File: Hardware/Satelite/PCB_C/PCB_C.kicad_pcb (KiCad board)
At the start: 2 copper layers, 54 x 54 mm, 50 parts, among them IC1 MCP1501T-33E_CHY, IC2 IS25LP080D-JULE-TR, IC3 BQ24392RSER, IC4 MS563702BA03-50, IC5 BMX055, J1 Conn_01x06, J2 JUMPER, J3 Conector_PCB_B-C, J4 Conector_Expansion_CanSat, J5 USB_B_Micro, Q1 BC817, U1 NTB0104BQ,115, U2 TCA9802DGKR, U3 STM32F303RETx, U4 NTB0104BQ,115, U5 SN74LVC1G3157DCKR, U6 Si7006-A20-IM1, Y1 LFXTAL016178, Y2 Crystal

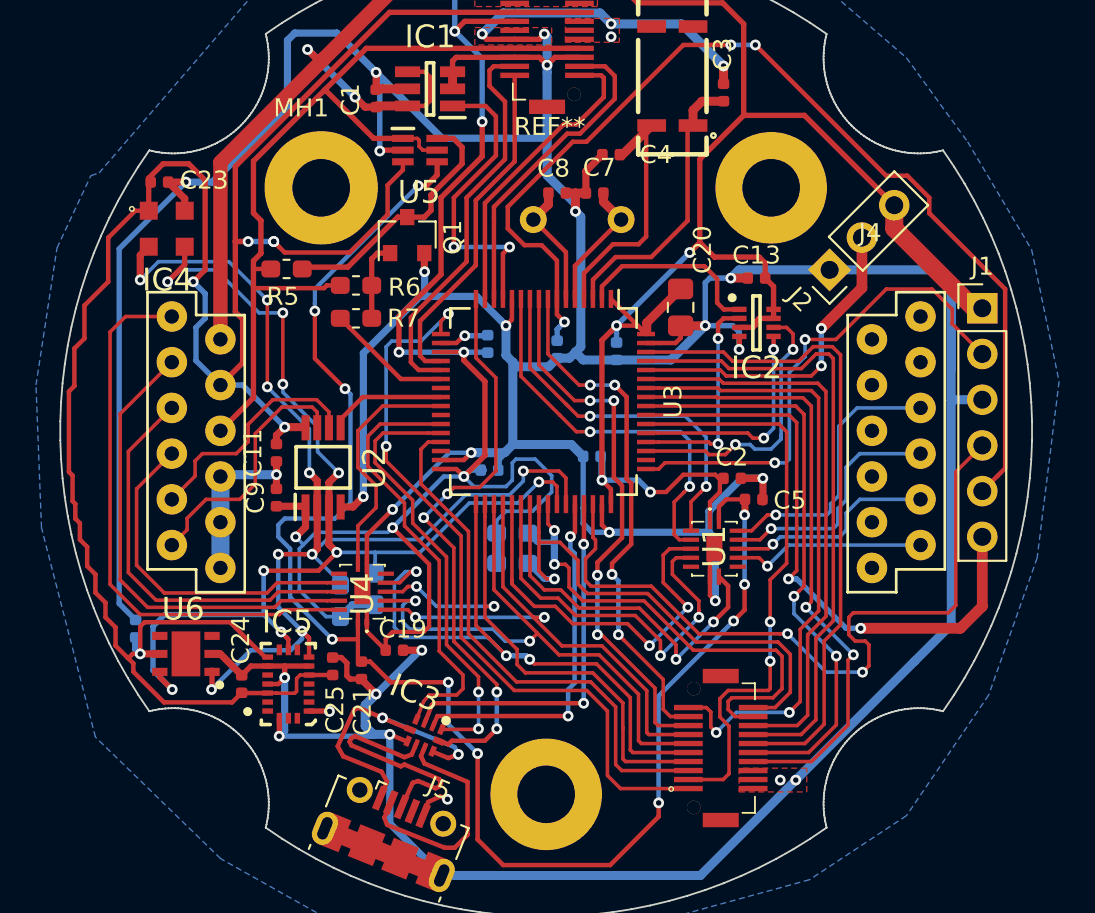
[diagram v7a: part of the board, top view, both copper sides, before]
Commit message: Pequeñas mejoras en PCB_C
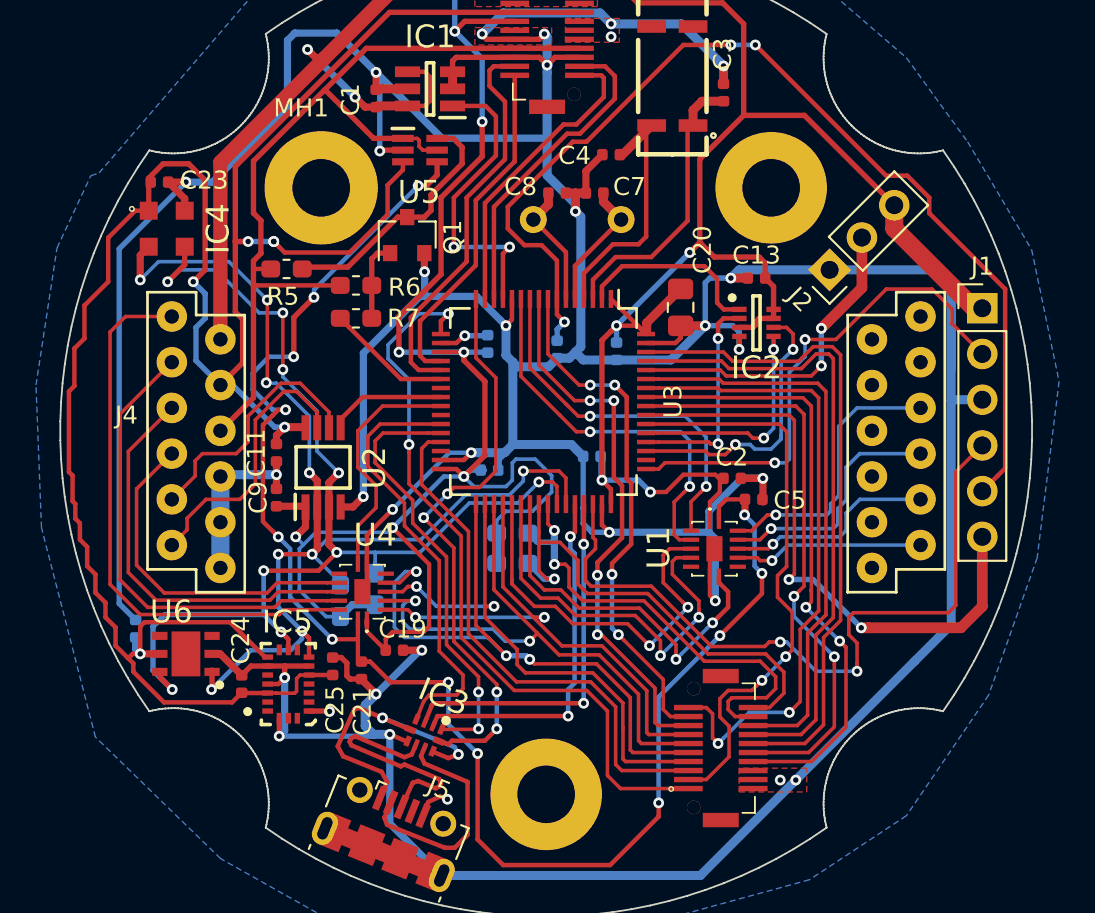
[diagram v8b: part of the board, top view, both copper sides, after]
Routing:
- net /SCL_CHG: track 27.7 -> 26.3 mm
- net /SDA_CHG: track 28.4 -> 27.2 mm
- net VDD: track 87.3 -> 88.5 mm, vias 10 -> 12
- net /SDA_EXT: track 14.3 -> 15.4 mm
- net /SCL_EXT: track 13.2 -> 14.3 mm
- net /SWDIO: track 41.7 -> 40.8 mm
- net /GPOUT: track 35.1 -> 35.9 mm
